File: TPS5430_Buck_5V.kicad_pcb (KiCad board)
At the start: 2 copper layers, 20 parts, among them J1 694103107102, J2 Conn_01x02_Pin, U1 TPS54308

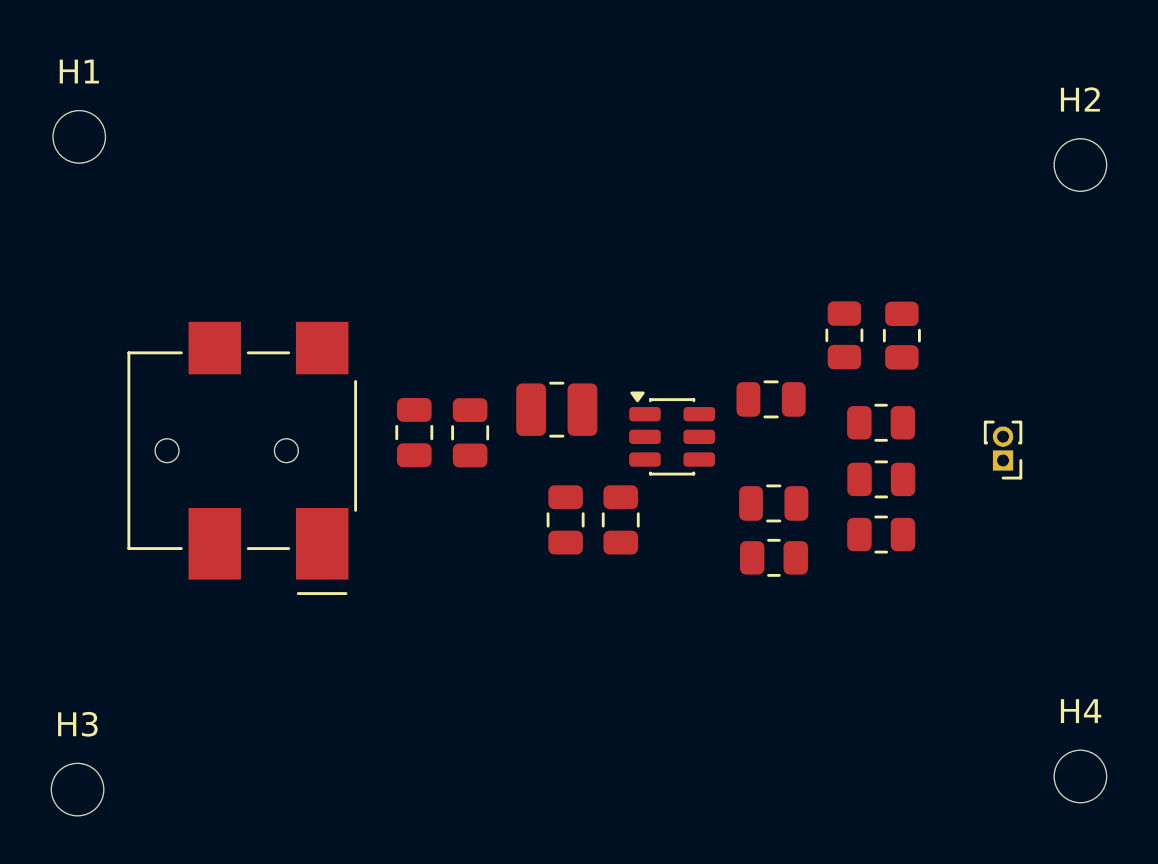
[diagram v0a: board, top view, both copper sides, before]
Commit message: redo component placement and finish routing
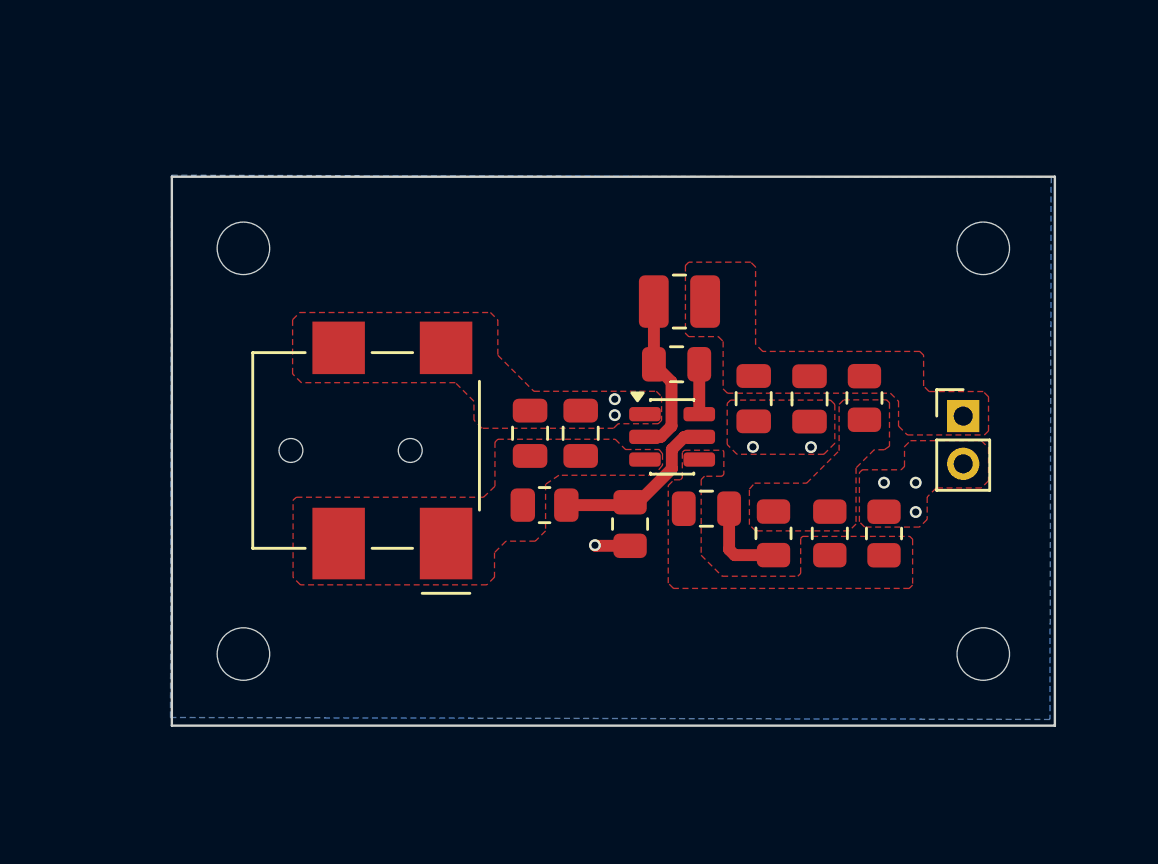
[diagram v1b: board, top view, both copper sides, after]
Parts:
- J2: footprint Connector_PinHeader_1.00mm:PinHeader_1x02_P1.00mm_Vertical -> Connector_PinHeader_2.00mm:PinHeader_1x02_P2.00mm_Vertical
- moved R4 14.4 mm to (114.6, 90.8), turned to 0 degrees
- moved C4 14.3 mm to (125.7, 86.3)
- moved C5 14.3 mm to (123.4, 86.3)
- moved R5 13.9 mm to (118.2, 91.6), turned to -90 degrees
- moved H3 8.98 mm to (102.0, 97.0)
- moved H1 8.32 mm to (102.0, 80.0)
- moved L1 6.85 mm to (120.3, 82.2), turned to 0 degrees
- moved H4 6.55 mm to (133.0, 97.0)
- moved R1 5.77 mm to (128.0, 86.3), turned to -90 degrees
- moved H2 5.36 mm to (133.0, 80.0)
- moved J1 5.19 mm to (106.5, 88.5)
- moved R3 4.64 mm to (128.8, 92.0), turned to 90 degrees
- moved C3 4.22 mm to (120.2, 84.9), turned to 0 degrees
- moved C2 4.00 mm to (116.1, 87.8), turned to -90 degrees
- moved C1 3.92 mm to (114.0, 87.8), turned to -90 degrees
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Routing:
- net Net-(U1-EN): track 0.00 -> 7.23 mm
- net Net-(U1-SW): track 0.00 -> 6.83 mm
- net Net-(C6-Pad2): track 0.00 -> 3.67 mm
- net Net-(U1-BOOT): track 0.00 -> 2.09 mm
- net GND: track 0.00 -> 1.48 mm, vias 0 -> 8
- added copper zone on B.Cu, net GND
- added copper zone on F.Cu, net GND
- added copper zone on F.Cu, net Net-(R1-Pad2)
- added copper zone on F.Cu, net Net-(U1-FB)
- added copper zone on F.Cu, net VIN
- added copper zone on F.Cu, net VOUT
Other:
- board outline added: 37 x 23 mm

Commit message: add texts in silkscreen
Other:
- board text added: "+"
- board text added: "-"
- board text added: "4/10/26"
- board text added: "Buck Convertor (12V to 5V 3A)"
- board text added: "INPUT"
- board text added: "OUTPUT"
- board text added: "V0.0.0"
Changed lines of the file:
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@@
 		(capping no)
 		(filling no)
-		(zone_defaults)
 		(pcbplotparams
 			(layerselection 0x00000000_00000000_55555555_5755f5ff)
@@
 			(at 0.02 -2.35 0)
 			(layer "F.Fab")
-			(hide yes)
 			(effects
 				(font
-					(size 1 1)
+					(size 0.8 0.8)
 					(thickness 0.15)
 				)
@@
 		(layer "Edge.Cuts")
 	)
+	(gr_text "INPUT"
+		(at 105.75 82.44 0)
+		(layer "F.SilkS")
+		(effects
+			(font
+				(size 0.8 0.8)
+				(thickness 0.1)
+			)
+			(justify left bottom)
+		)
+	)
+	(gr_text "OUTPUT"
+		(at 130.6 85.04 0)
+		(layer "F.SilkS")
+		(effects
+			(font
+				(size 0.8 0.8)
+				(thickness 0.1)
+			)
+			(justify left bottom)
+		)
+	)
+	(gr_text "+"
+		(at 134.68 87.46 90)
+		(layer "F.SilkS")
+		(effects
+			(font
+				(size 0.8 0.8)
+				(thickness 0.1)
+			)
+			(justify left bottom)
+		)
+	)
+	(gr_text "-"
+		(at 134.71 89.78 90)
+		(layer "F.SilkS")
+		(effects
+			(font
+				(size 0.8 0.8)
+				(thickness 0.1)
+			)
+			(justify left bottom)
+		)
+	)
+	(gr_text "Buck Convertor (12V to 5V 3A)"
+		(at 126.54 78.94 0)
+		(layer "B.SilkS")
+		(effects
+			(font
+				(size 0.8 0.8)
+				(thickness 0.1)
+			)
+			(justify left bottom mirror)
+		)
+	)
+	(gr_text "4/10/26"
+		(at 109.89 97.55 0)
+		(layer "B.SilkS")
+		(effects
+			(font
+				(size 0.8 0.8)
+				(thickness 0.1)
+				(italic yes)
+			)
+			(justify left bottom mirror)
+		)
+	)
+	(gr_text "V0.0.0"
+		(at 118.3 80.51 0)
+		(layer "B.SilkS")
+		(effects
+			(font
+				(size 0.8 0.8)
+				(thickness 0.1)
+				(italic yes)
+			)
+			(justify left bottom mirror)
+		)
+	)
 	(dimension

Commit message: add thermal reliefs to avoid tombstoning
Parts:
- moved R1 4.84 mm to (126.9, 91.0), turned to 180 degrees
- moved R6 1.65 mm to (123.3, 93.3), turned to 0 degrees
- moved R3 1.41 mm to (130.2, 92.4)
- moved R2 1.41 mm to (126.9, 93.3), turned to 0 degrees
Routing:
- net Net-(U1-FB): track 0.00 -> 17.4 mm
- net VOUT: track 0.00 -> 9.16 mm
- net Net-(R1-Pad2): track 0.00 -> 4.15 mm
- net Net-(U1-SW): track 6.83 -> 4.20 mm
- net Net-(C6-Pad2): track 3.67 -> 2.39 mm
- net GND: vias 8 -> 10
- added copper zone on F.Cu, net Net-(U1-SW)
- removed copper zone on F.Cu, net Net-(R1-Pad2)
- removed copper zone on F.Cu, net Net-(U1-FB)
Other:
- board text added: "5/10/26"
- board text removed: "4/10/26"
